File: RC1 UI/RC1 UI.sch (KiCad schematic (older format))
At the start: 59 parts, among them J1 KEYPAD, J2 RC1_UI_Port, J3 COM, J4 TAPE, M1 Mounting, M2 Mounting, M3 Mounting, M4 Mounting, Q1 2N3904, Q2 2N3904, Q3 2N3904, Q4 2N3904, Q5 2N3904, Q6 2N3904, U1 74LS138, U2 74LS138, U3 74LS01, U4 74LS00, U5 74LS04, U6 74LS244

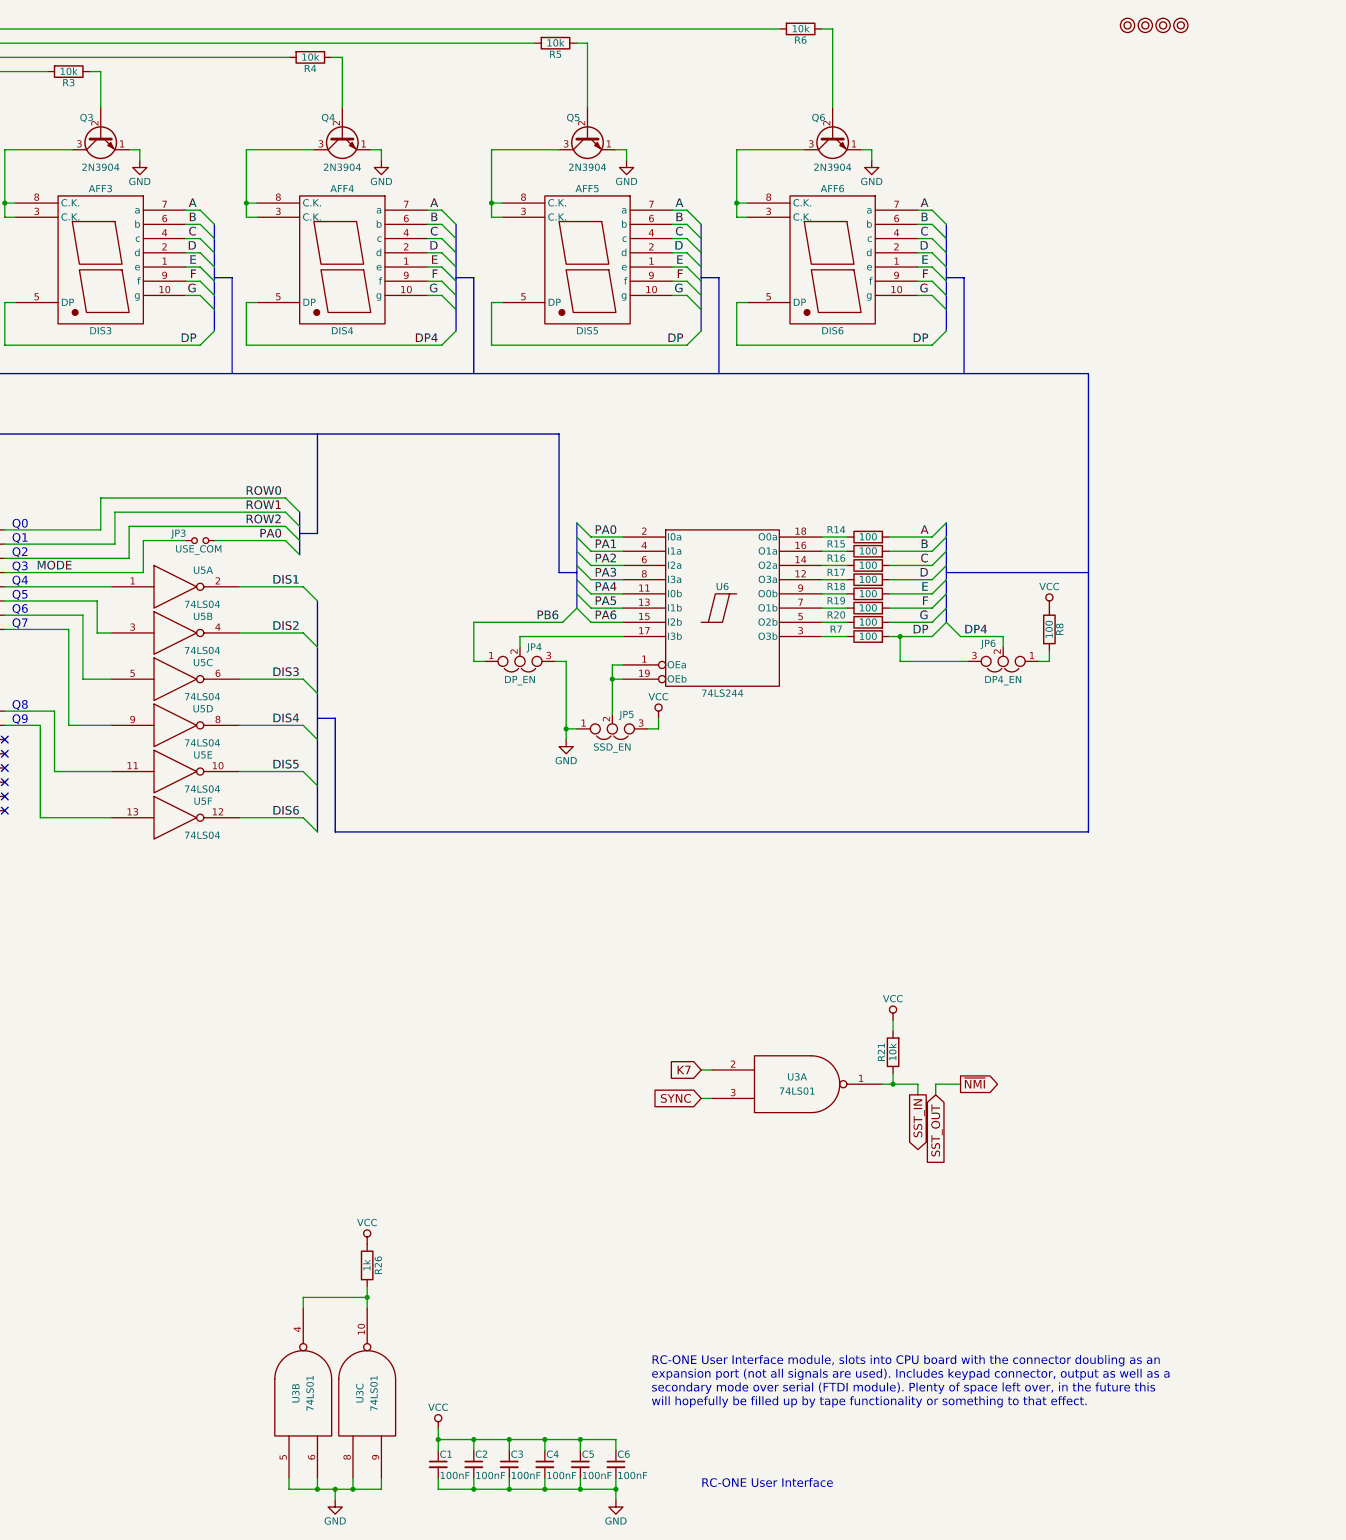
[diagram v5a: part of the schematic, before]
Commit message: Added diodes to solve display glitch
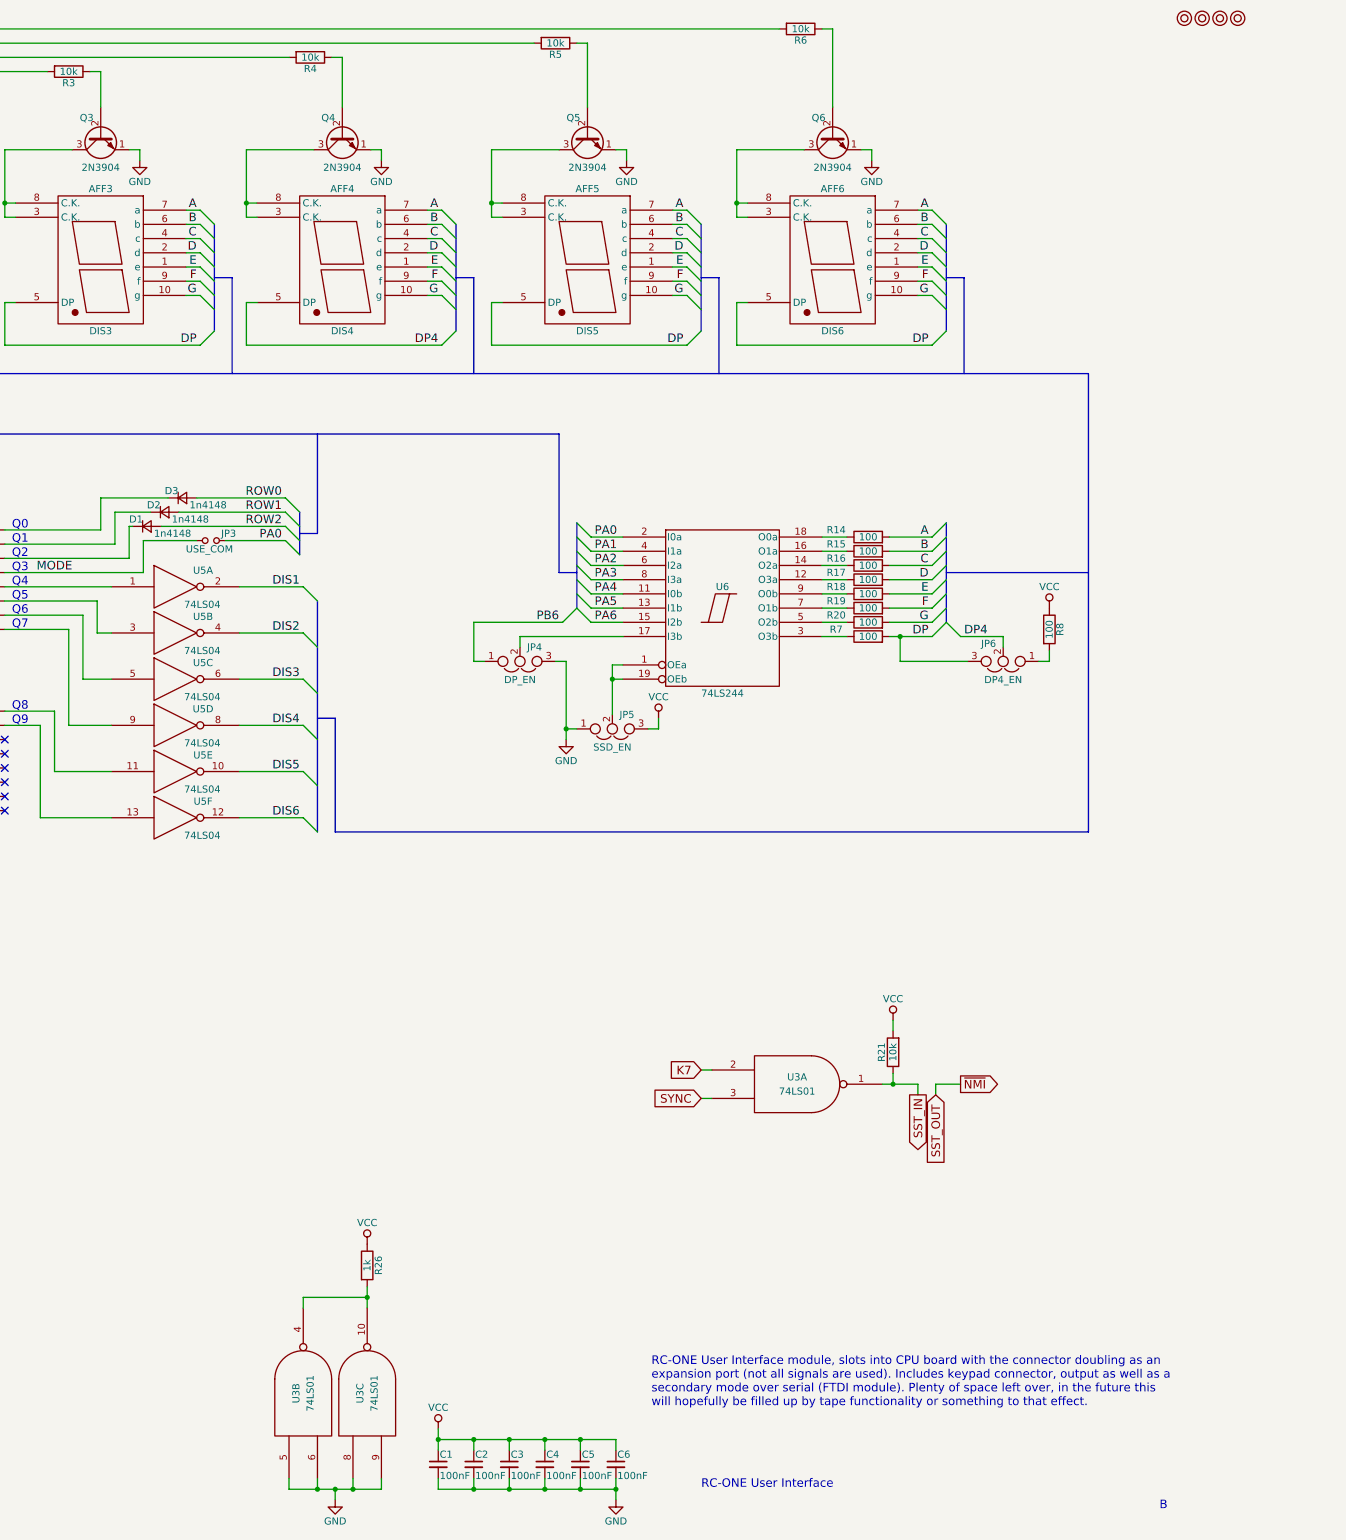
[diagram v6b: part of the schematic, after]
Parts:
- added D1, D2, D3: 1n4148, symbol D_Small
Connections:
- net ROW0: now also D3.2 (A); no longer U1.15 (O0)
- net ROW1: now also D2.2 (A); no longer U1.14 (O1)
- net ROW2: now also D1.2 (A); no longer U1.13 (O2)
- new net: D1.1 (K), U1.13 (O2)
- new net: D2.1 (K), U1.14 (O1)
- new net: D3.1 (K), U1.15 (O0)
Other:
- moved on the sheet: JP3

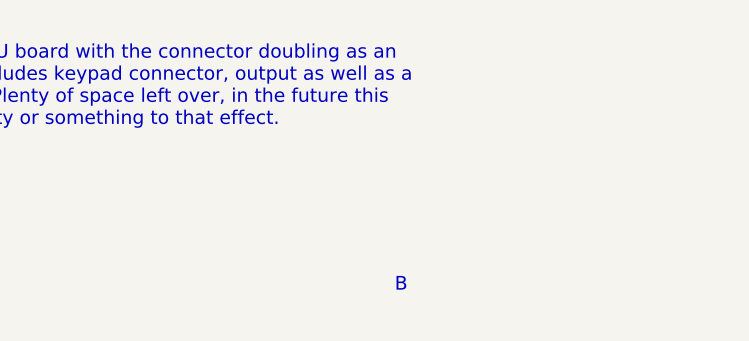
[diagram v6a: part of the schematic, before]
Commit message: Added diodes to UI board
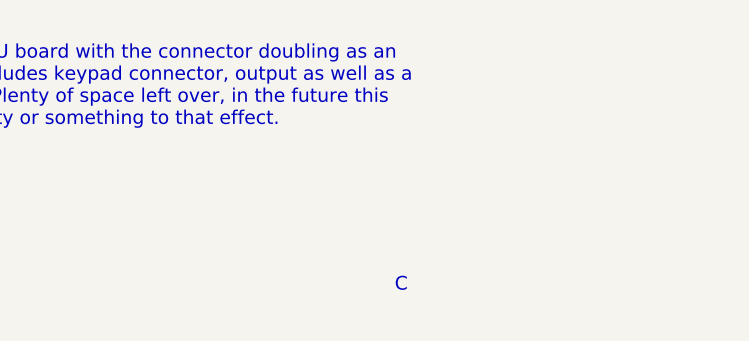
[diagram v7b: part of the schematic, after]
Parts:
- D1, D2, D3: footprint (none) -> Diodes_THT:D_DO-35_SOD27_P7.62mm_Horizontal
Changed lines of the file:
@@
 	1200 1250 1300 1150
 $Comp
-L GND #PWR5
+L GND #PWR01
 U 1 1 5D64EB6A
 P 3250 1125
-F 0 "#PWR5" H 3250 875 50  0001 C CNN
+F 0 "#PWR01" H 3250 875 50  0001 C CNN
 F 1 "GND" H 3250 975 50  0000 C CNN
 F 2 "" H 3250 1125 50  0001 C CNN
@@
 	1200 1950 1300 1850
 $Comp
-L VCC #PWR2
+L VCC #PWR02
 U 1 1 5D651400
 P 2200 850
-F 0 "#PWR2" H 2200 700 50  0001 C CNN
+F 0 "#PWR02" H 2200 700 50  0001 C CNN
 F 1 "VCC" H 2200 1000 50  0000 C CNN
 F 2 "" H 2200 850 50  0001 C CNN
@@
 $EndComp
 $Comp
-L VCC #PWR27
+L VCC #PWR03
 U 1 1 5D66F47C
 P 13525 7625
-F 0 "#PWR27" H 13525 7475 50  0001 C CNN
+F 0 "#PWR03" H 13525 7475 50  0001 C CNN
 F 1 "VCC" H 13525 7775 50  0000 C CNN
 F 2 "" H 13525 7625 50  0001 C CNN
@@
 $EndComp
 $Comp
-L GND #PWR8
+L GND #PWR04
 U 1 1 5D683925
 P 3450 3975
-F 0 "#PWR8" H 3450 3725 50  0001 C CNN
+F 0 "#PWR04" H 3450 3725 50  0001 C CNN
 F 1 "GND" H 3450 3825 50  0000 C CNN
 F 2 "" H 3450 3975 50  0001 C CNN
@@
 $EndComp
 $Comp
-L VCC #PWR3
+L VCC #PWR05
 U 1 1 5D68403B
 P 2250 4075
-F 0 "#PWR3" H 2250 3925 50  0001 C CNN
+F 0 "#PWR05" H 2250 3925 50  0001 C CNN
 F 1 "VCC" H 2250 4225 50  0000 C CNN
 F 2 "" H 2250 4075 50  0001 C CNN
@@
 $EndComp
 $Comp
-L GND #PWR23
+L GND #PWR06
 U 1 1 5D68643F
 P 11575 11000
-F 0 "#PWR23" H 11575 10750 50  0001 C CNN
+F 0 "#PWR06" H 11575 10750 50  0001 C CNN
 F 1 "GND" H 11575 10850 50  0000 C CNN
 F 2 "" H 11575 11000 50  0001 C CNN
@@
 $EndComp
 $Comp
-L VCC #PWR21
+L VCC #PWR07
 U 1 1 5D6865DB
 P 10325 10500
-F 0 "#PWR21" H 10325 10350 50  0001 C CNN
+F 0 "#PWR07" H 10325 10350 50  0001 C CNN
 F 1 "VCC" H 10325 10650 50  0000 C CNN
 F 2 "" H 10325 10500 50  0001 C CNN
@@
 PB7
 $Comp
-L GND #PWR4
+L GND #PWR08
 U 1 1 5D66CD2E
 P 2250 6175
-F 0 "#PWR4" H 2250 5925 50  0001 C CNN
+F 0 "#PWR08" H 2250 5925 50  0001 C CNN
 F 1 "GND" H 2250 6025 50  0000 C CNN
 F 2 "" H 2250 6175 50  0001 C CNN
@@
 $EndComp
 $Comp
-L VCC #PWR1
+L VCC #PWR09
 U 1 1 5D7172BC
 P 1675 9150
-F 0 "#PWR1" H 1675 9000 50  0001 C CNN
+F 0 "#PWR09" H 1675 9000 50  0001 C CNN
 F 1 "VCC" H 1675 9300 50  0000 C CNN
 F 2 "" H 1675 9150 50  0001 C CNN
@@
 RX
 $Comp
-L GND #PWR18
+L GND #PWR010
 U 1 1 5D72ADA8
 P 9600 11000
-F 0 "#PWR18" H 9600 10750 50  0001 C CNN
+F 0 "#PWR010" H 9600 10750 50  0001 C CNN
 F 1 "GND" H 9600 10850 50  0000 C CNN
 F 2 "" H 9600 11000 50  0001 C CNN
@@
 $EndComp
 $Comp
-L VCC #PWR11
+L VCC #PWR011
 U 1 1 5D72E978
 P 5575 7600
-F 0 "#PWR11" H 5575 7450 50  0001 C CNN
+F 0 "#PWR011" H 5575 7450 50  0001 C CNN
 F 1 "VCC" H 5575 7750 50  0000 C CNN
 F 2 "" H 5575 7600 50  0001 C CNN
@@
 $EndComp
 $Comp
-L GND #PWR15
+L GND #PWR012
 U 1 1 5D72F4FA
 P 6025 8550
-F 0 "#PWR15" H 6025 8300 50  0001 C CNN
+F 0 "#PWR012" H 6025 8300 50  0001 C CNN
 F 1 "GND" H 6025 8400 50  0000 C CNN
 F 2 "" H 6025 8550 50  0001 C CNN
@@
 NoConn ~ 2325 4400
 $Comp
-L GND #PWR6
+L GND #PWR013
 U 1 1 5D737105
 P 3350 6175
-F 0 "#PWR6" H 3350 5925 50  0001 C CNN
+F 0 "#PWR013" H 3350 5925 50  0001 C CNN
 F 1 "GND" H 3350 6025 50  0000 C CNN
 F 2 "" H 3350 6175 50  0001 C CNN
@@
 $EndComp
 $Comp
-L VCC #PWR19
+L VCC #PWR014
 U 1 1 5D745522
 P 9825 9200
-F 0 "#PWR19" H 9825 9050 50  0001 C CNN
+F 0 "#PWR014" H 9825 9050 50  0001 C CNN
 F 1 "VCC" H 9825 9350 50  0000 C CNN
 F 2 "" H 9825 9200 50  0001 C CNN
@@
 NoConn ~ 7275 6150
 $Comp
-L GND #PWR14
+L GND #PWR015
 U 1 1 5D922599
 P 6000 6225
-F 0 "#PWR14" H 6000 5975 50  0001 C CNN
+F 0 "#PWR015" H 6000 5975 50  0001 C CNN
 F 1 "GND" H 6000 6075 50  0000 C CNN
 F 2 "" H 6000 6225 50  0001 C CNN
@@
 Q7
 $Comp
-L GND #PWR13
+L GND #PWR016
 U 1 1 5D93B7A1
 P 6000 4950
-F 0 "#PWR13" H 6000 4700 50  0001 C CNN
+F 0 "#PWR016" H 6000 4700 50  0001 C CNN
 F 1 "GND" H 6000 4800 50  0000 C CNN
 F 2 "" H 6000 4950 50  0001 C CNN
@@
 $EndComp
 $Comp
-L VCC #PWR12
+L VCC #PWR017
 U 1 1 5D93B7AB
 P 6000 4600
-F 0 "#PWR12" H 6000 4450 50  0001 C CNN
+F 0 "#PWR017" H 6000 4450 50  0001 C CNN
 F 1 "VCC" H 6000 4750 50  0000 C CNN
 F 2 "" H 6000 4600 50  0001 C CNN
@@
 $EndComp
 $Comp
-L GND #PWR16
+L GND #PWR018
 U 1 1 5D991AFE
 P 6525 1575
-F 0 "#PWR16" H 6525 1325 50  0001 C CNN
+F 0 "#PWR018" H 6525 1325 50  0001 C CNN
 F 1 "GND" H 6525 1425 50  0000 C CNN
 F 2 "" H 6525 1575 50  0001 C CNN
@@
 $EndComp
 $Comp
-L GND #PWR10
+L GND #PWR019
 U 1 1 5D9943DA
 P 4825 1575
-F 0 "#PWR10" H 4825 1325 50  0001 C CNN
+F 0 "#PWR019" H 4825 1325 50  0001 C CNN
 F 1 "GND" H 4825 1425 50  0000 C CNN
 F 2 "" H 4825 1575 50  0001 C CNN
@@
 $EndComp
 $Comp
-L GND #PWR17
+L GND #PWR020
 U 1 1 5D994526
 P 8225 1575
-F 0 "#PWR17" H 8225 1325 50  0001 C CNN
+F 0 "#PWR020" H 8225 1325 50  0001 C CNN
 F 1 "GND" H 8225 1425 50  0000 C CNN
 F 2 "" H 8225 1575 50  0001 C CNN
@@
 $EndComp
 $Comp
-L GND #PWR20
+L GND #PWR021
 U 1 1 5D994765
 P 9925 1575
-F 0 "#PWR20" H 9925 1325 50  0001 C CNN
+F 0 "#PWR021" H 9925 1325 50  0001 C CNN
 F 1 "GND" H 9925 1425 50  0000 C CNN
 F 2 "" H 9925 1575 50  0001 C CNN
@@
 $EndComp
 $Comp
-L GND #PWR24
+L GND #PWR022
 U 1 1 5D994D28
 P 11650 1575
-F 0 "#PWR24" H 11650 1325 50  0001 C CNN
+F 0 "#PWR022" H 11650 1325 50  0001 C CNN
 F 1 "GND" H 11650 1425 50  0000 C CNN
 F 2 "" H 11650 1575 50  0001 C CNN
@@
 $EndComp
 $Comp
-L GND #PWR26
+L GND #PWR023
 U 1 1 5D99524C
 P 13375 1575
-F 0 "#PWR26" H 13375 1325 50  0001 C CNN
+F 0 "#PWR023" H 13375 1325 50  0001 C CNN
 F 1 "GND" H 13375 1425 50  0000 C CNN
 F 2 "" H 13375 1575 50  0001 C CNN
@@
 $EndComp
 $Comp
-L GND #PWR22
+L GND #PWR024
 U 1 1 5D9A6D42
 P 11225 5650
-F 0 "#PWR22" H 11225 5400 50  0001 C CNN
+F 0 "#PWR024" H 11225 5400 50  0001 C CNN
 F 1 "GND" H 11225 5500 50  0000 C CNN
 F 2 "" H 11225 5650 50  0001 C CNN
@@
 $EndComp
 $Comp
-L VCC #PWR25
+L VCC #PWR025
 U 1 1 5D9A70E1
 P 11875 5500
-F 0 "#PWR25" H 11875 5350 50  0001 C CNN
+F 0 "#PWR025" H 11875 5350 50  0001 C CNN
 F 1 "VCC" H 11875 5650 50  0000 C CNN
 F 2 "" H 11875 5500 50  0001 C CNN
@@
 $EndComp
 $Comp
-L VCC #PWR28
+L VCC #PWR026
 U 1 1 5D9C6E3B
 P 14625 4725
-F 0 "#PWR28" H 14625 4575 50  0001 C CNN
+F 0 "#PWR026" H 14625 4575 50  0001 C CNN
 F 1 "VCC" H 14625 4875 50  0000 C CNN
 F 2 "" H 14625 4725 50  0001 C CNN
@@
 $EndComp
 $Comp
-L GND #PWR9
+L GND #PWR027
 U 1 1 5DA389CD
 P 3800 9525
-F 0 "#PWR9" H 3800 9275 50  0001 C CNN
+F 0 "#PWR027" H 3800 9275 50  0001 C CNN
 F 1 "GND" H 3800 9375 50  0000 C CNN
 F 2 "" H 3800 9525 50  0001 C CNN
@@
 $EndComp
 $Comp
-L VCC #PWR7
+L VCC #PWR028
 U 1 1 5DA611F9
 P 3350 9100
-F 0 "#PWR7" H 3350 8950 50  0001 C CNN
+F 0 "#PWR028" H 3350 8950 50  0001 C CNN
 F 1 "VCC" H 3350 9250 50  0000 C CNN
 F 2 "" H 3350 9100 50  0001 C CNN
@@
 	5775 7575 5775 8375
 Text Notes 15400 11075 0    60   ~ 0
-B
+C
 $Comp
 L D_Small D1
@@
 F 0 "D1" H 8150 4200 50  0000 L CNN
 F 1 "1n4148" H 8325 4100 50  0000 L CNN
-F 2 "" V 8275 4150 50  0001 C CNN
+F 2 "Diodes_THT:D_DO-35_SOD27_P7.62mm_Horizontal" V 8275 4150 50  0001 C CNN
 F 3 "" V 8275 4150 50  0001 C CNN
 	1    8275 4150
@@
 F 0 "D2" H 8275 4100 50  0000 L CNN
 F 1 "1n4148" H 8450 4000 50  0000 L CNN
-F 2 "" V 8400 4050 50  0001 C CNN
+F 2 "Diodes_THT:D_DO-35_SOD27_P7.62mm_Horizontal" V 8400 4050 50  0001 C CNN
 F 3 "" V 8400 4050 50  0001 C CNN
 	1    8400 4050
@@
 F 0 "D3" H 8400 4000 50  0000 L CNN
 F 1 "1n4148" H 8575 3900 50  0000 L CNN
-F 2 "" V 8525 3950 50  0001 C CNN
+F 2 "Diodes_THT:D_DO-35_SOD27_P7.62mm_Horizontal" V 8525 3950 50  0001 C CNN
 F 3 "" V 8525 3950 50  0001 C CNN
 	1    8525 3950

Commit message: Changed UI resistors to horizontal
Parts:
- removed J4: TAPE, Pin_Headers:Pin_Header_Straight_1x04_Pitch2.54mm, symbol Conn_01x04
- added C10: 500nF, Capacitors_THT:C_Disc_D4.7mm_W2.5mm_P5.00mm, symbol C
- added C11: 100nF, Capacitors_THT:C_Disc_D4.7mm_W2.5mm_P5.00mm, symbol C
- added C7, C9: 50nF, Capacitors_THT:C_Disc_D4.7mm_W2.5mm_P5.00mm, symbol C
- added C8: 68nF, Capacitors_THT:C_Disc_D4.7mm_W2.5mm_P5.00mm, symbol C
- added D4: DATA_IN, LEDs:LED_D5.0mm, symbol LED_Small
- added D5, D6, D7: 1n914, Diodes_THT:D_DO-35_SOD27_P7.62mm_Horizontal, symbol D_Small
- added J4: TAPE, TRS:Tayda_3.5mm_stereo_TRS_jack_A-853, symbol TRS_3.5mm
- added Q7, Q8, Q9: 2N3904, TO_SOT_Packages_THT:TO-92_Molded_Narrow, symbol 2N3904
- added R10: 100, Resistors_THT:R_Axial_DIN0207_L6.3mm_D2.5mm_P10.16mm_Horizontal, symbol R
- added R11, R33: 1k5, Resistors_THT:R_Axial_DIN0207_L6.3mm_D2.5mm_P10.16mm_Horizontal, symbol R
- added R12: 6k2, Resistors_THT:R_Axial_DIN0207_L6.3mm_D2.5mm_P10.16mm_Horizontal, symbol R
- added R24: 3k3, Resistors_THT:R_Axial_DIN0207_L6.3mm_D2.5mm_P10.16mm_Horizontal, symbol R
- added R27: 2k7, Resistors_THT:R_Axial_DIN0207_L6.3mm_D2.5mm_P10.16mm_Horizontal, symbol R
- added R28, R34, R9: 10k, Resistors_THT:R_Axial_DIN0207_L6.3mm_D2.5mm_P10.16mm_Horizontal, symbol R
- added R29, R30, R31: 1k, Resistors_THT:R_Axial_DIN0207_L6.3mm_D2.5mm_P10.16mm_Horizontal, symbol R
- added R32: 6k8, Resistors_THT:R_Axial_DIN0207_L6.3mm_D2.5mm_P10.16mm_Horizontal, symbol R
- added R35: 51k, Resistors_THT:R_Axial_DIN0207_L6.3mm_D2.5mm_P10.16mm_Horizontal, symbol R
- added R36: 2k2, Resistors_THT:R_Axial_DIN0207_L6.3mm_D2.5mm_P10.16mm_Horizontal, symbol R
- R1, R2, R3, R4, R5, R6: footprint Resistors_THT:R_Axial_DIN0207_L6.3mm_D2.5mm_P5.08mm_Vertical -> Resistors_THT:R_Axial_DIN0207_L6.3mm_D2.5mm_P10.16mm_Horizontal
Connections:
- net GND: now also C7.1, C8.1, C9.1, D6.2 (A), D7.2 (A), J4.1, Q7.1 (E), Q8.1 (E), Q9.1 (E), R10.2, R12.2, R28.1, R32.2, R34.2
- net VCC: now also R11.2, R27.2, R33.2, R35.1
- net TO_TAPE: now reaches R22.1, U3.13
- net TO_TAPE: now also R9.2
- net FROM_TAPE: now reaches U4.13
- net FROM_TAPE: now also Q7.3 (C), R11.1
- new net: C11.1, R36.2
- new net: D7.1 (K), Q9.2 (B), R34.1, R35.2, R36.1
- new net: C10.2, Q9.3 (C), R33.1
- new net: C10.1, D5.2 (A), D6.1 (K)
- new net: C9.2, D5.1 (K), R31.1, R32.1
- new net: C8.2, R30.1, R31.2
- new net: C7.2, R29.1, R30.2
- new net: Q8.2 (B), R28.2, R29.2
- new net: D4.1 (K), Q8.3 (C), R24.1
- new net: D4.2 (A), R27.1
- new net: Q7.2 (B), R12.1, R24.2
- new net TAPE_EAR: C11.2, J4.2, J4.3
- new net TAPE_MIC: J4.4, J4.5, R10.1, R9.1
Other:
- note added: "Uses the same cable setup as found\non the ZX Spectrum +3, with EAR\nis data from tape to computer -\nMIC is data out to tape."
- moved on the sheet: AFF1, AFF2, AFF3, AFF4, AFF5, AFF6, C1, C2, C3, C4, C5, C6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
